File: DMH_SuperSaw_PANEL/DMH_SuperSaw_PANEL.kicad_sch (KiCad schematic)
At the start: 29 parts, among them J0 Panel_GND_Solder_Wire_Pad

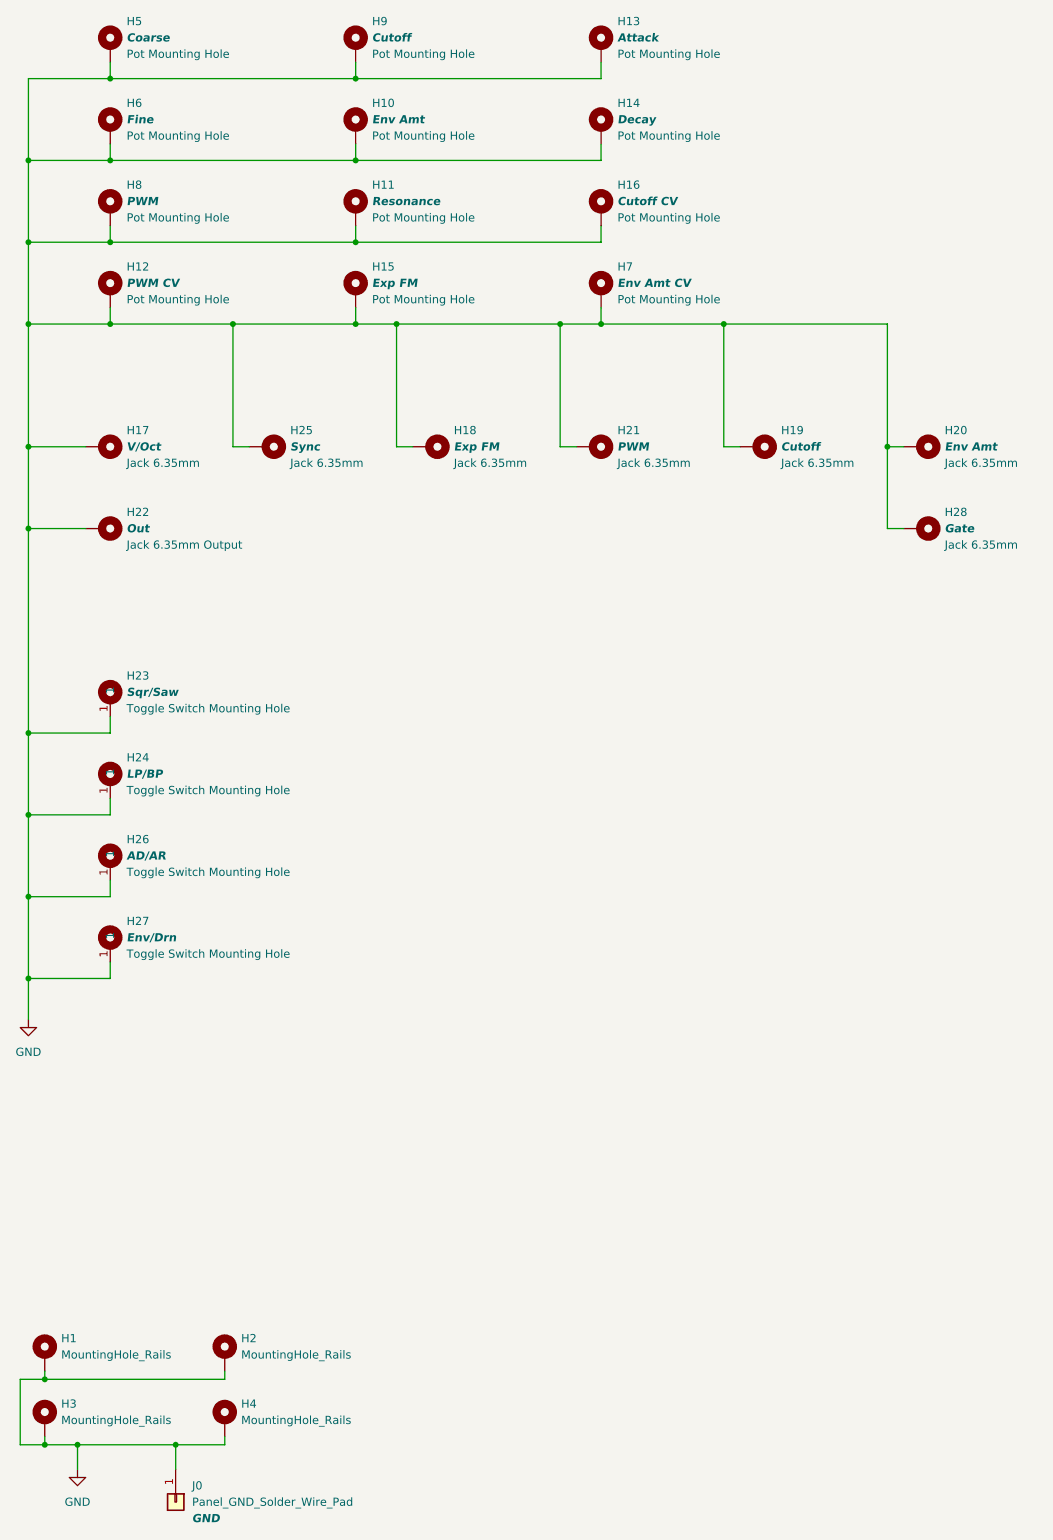
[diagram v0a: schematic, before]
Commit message: Designed front panel
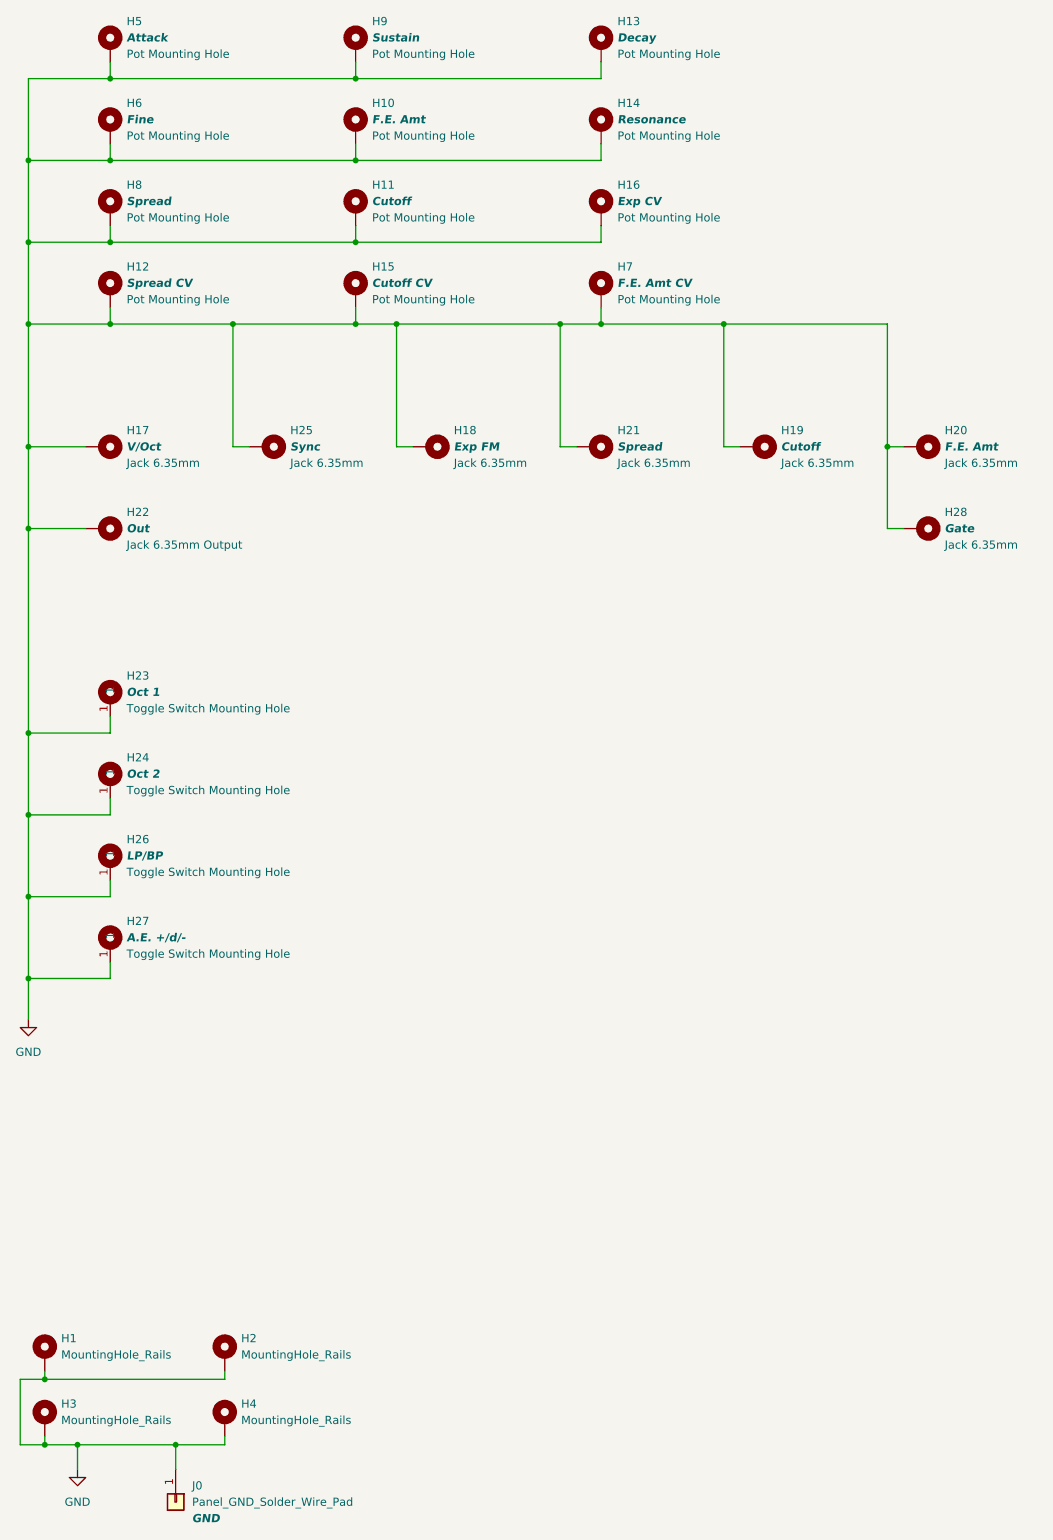
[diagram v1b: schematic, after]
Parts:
- H10: value Env Amt -> F.E. Amt; footprint SynthStuff:Pot_Cutout_Tiny_attv_P110KH1 -> SynthStuff:Pot_Cutout_Small_attv_P110KH1
- H11: value Resonance -> Cutoff
- H12: value PWM CV -> Spread CV
- H13: value Attack -> Decay
- H14: value Decay -> Resonance
- H15: value Exp FM -> Cutoff CV
- H16: value Cutoff CV -> Exp CV
- H20: value Env Amt -> F.E. Amt
- H21, H8: value PWM -> Spread
- H23: value Sqr/Saw -> Oct 1
- H24: value LP/BP -> Oct 2
- H26: value AD/AR -> LP/BP
- H27: value Env/Drn -> A.E. +/d/-
- H5: value Coarse -> Attack
- H7: value Env Amt CV -> F.E. Amt CV
- H9: value Cutoff -> Sustain
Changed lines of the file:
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@@
 			)
 		)
-		(property "Value" "LP/BP"
+		(property "Value" "Oct 2"
 			(at 40.64 165.1 0)
 			(effects
@@
 			)
 		)
-		(property "Value" "Coarse"
-			(at 40.64 50.7999 0)
+		(property "Value" "Attack"
+			(at 40.64 50.8 0)
 			(effects
 				(font
@@
 			)
 		)
-		(property "Value" "AD/AR"
+		(property "Value" "LP/BP"
 			(at 40.64 177.8 0)
 			(effects
@@
 			)
 		)
-		(property "Value" "Exp FM"
+		(property "Value" "Cutoff CV"
 			(at 78.74 88.9 0)
 			(effects
@@
 			)
 		)
-		(property "Value" "PWM"
+		(property "Value" "Spread"
 			(at 40.64 76.2 0)
 			(effects
@@
 			)
 		)
-		(property "Value" "Sqr/Saw"
+		(property "Value" "Oct 1"
 			(at 40.64 152.4 0)
 			(effects
@@
 			)
 		)
-		(property "Value" "Attack"
+		(property "Value" "Decay"
 			(at 116.84 50.8 0)
 			(effects
@@
 			)
 		)
-		(property "Value" "Env Amt CV"
+		(property "Value" "F.E. Amt CV"
 			(at 116.84 88.9 0)
 			(effects
@@
 			)
 		)
-		(property "Value" "PWM"
+		(property "Value" "Spread"
 			(at 116.84 114.3 0)
 			(effects
@@
 			)
 		)
-		(property "Value" "Decay"
+		(property "Value" "Resonance"
 			(at 116.84 63.5 0)
 			(effects
@@
 			)
 		)
-		(property "Value" "Cutoff"
+		(property "Value" "Sustain"
 			(at 78.74 50.8 0)
 			(effects
@@
 			)
 		)
-		(property "Value" "Resonance"
+		(property "Value" "Cutoff"
 			(at 78.74 76.2 0)
 			(effects
@@
 			)
 		)
-		(property "Value" "Env Amt"
+		(property "Value" "F.E. Amt"
 			(at 167.64 114.3 0)
 			(effects
@@
 			)
 		)
-		(property "Value" "Env/Drn"
+		(property "Value" "A.E. +/d/-"
 			(at 40.64 190.5 0)
 			(effects
@@
 			)
 		)
-		(property "Value" "PWM CV"
+		(property "Value" "Spread CV"
 			(at 40.64 88.9 0)
 			(effects
@@
 			)
 		)
-		(property "Value" "Env Amt"
+		(property "Value" "F.E. Amt"
 			(at 78.74 63.5 0)
 			(effects
@@
 			)
 		)
-		(property "Footprint" "SynthStuff:Pot_Cutout_Tiny_attv_P110KH1"
+		(property "Footprint" "SynthStuff:Pot_Cutout_Small_attv_P110KH1"
 			(at 76.2 64.77 0)
 			(effects
@@
 			)
 		)
-		(property "Value" "Cutoff CV"
+		(property "Value" "Exp CV"
 			(at 116.84 76.2 0)
 			(effects

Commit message: Minor corrections
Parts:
- H13: value Decay -> Decay / Release
- H16: value Exp CV -> Exp FM CV
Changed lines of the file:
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@@
 			)
 		)
-		(property "Value" "Decay"
+		(property "Value" "Decay / Release"
 			(at 116.84 50.8 0)
 			(effects
@@
 			)
 		)
-		(property "Value" "Exp CV"
+		(property "Value" "Exp FM CV"
 			(at 116.84 76.2 0)
 			(effects
